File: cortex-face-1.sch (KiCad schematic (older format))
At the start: 14 parts

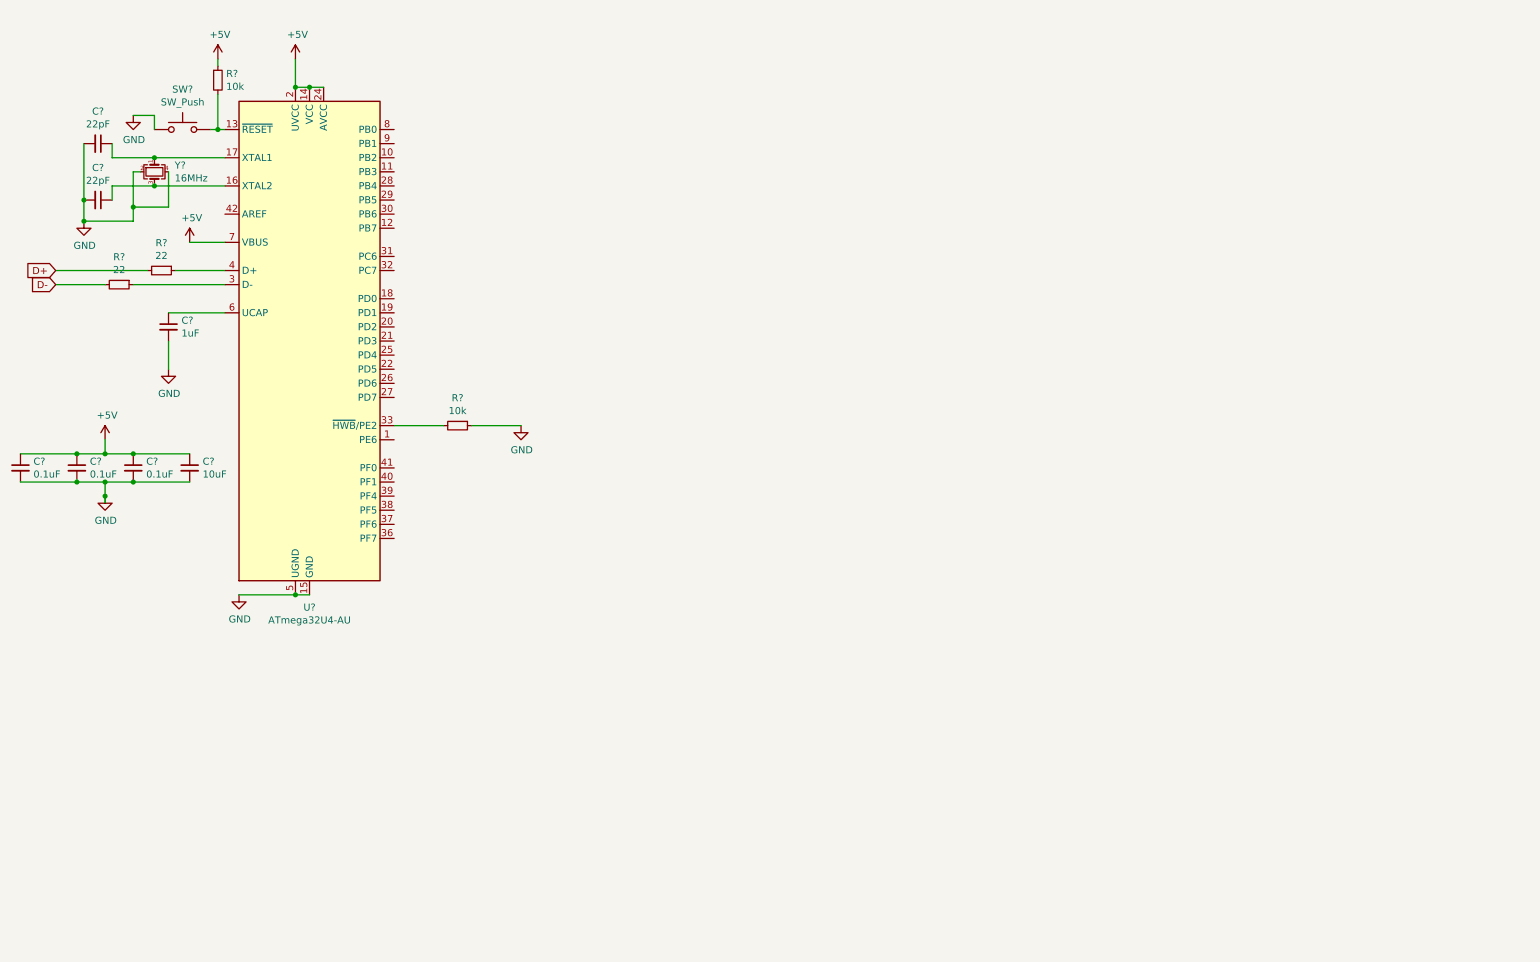
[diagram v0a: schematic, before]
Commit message: Basic 15x6 switch matrix
Switch matrix drawn with a simple rectangular matrix (15x6). MX only switches, no LED support.
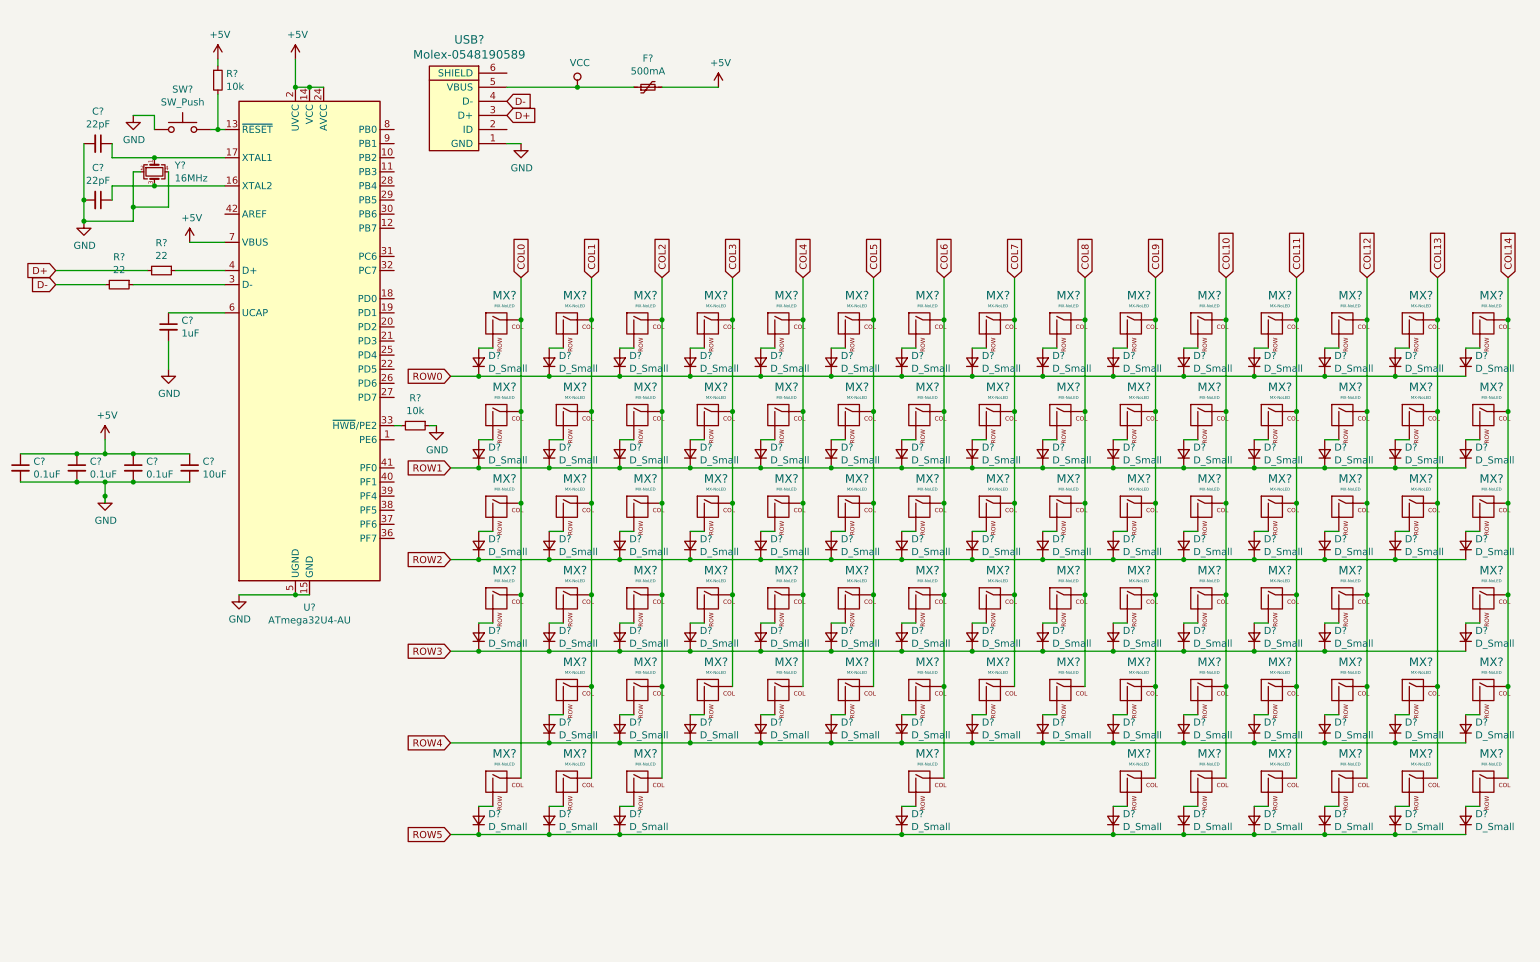
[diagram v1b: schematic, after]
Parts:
- added D? (x83): D_Small, symbol Device:D_Small
- added F?: 500mA, symbol Device:Polyfuse_Small
- added MX? (x83): MX-NoLED, symbol MX_Alps_Hybrid:MX-NoLED
- added USB?: Molex-0548190589, symbol random-keyboard-parts:Molex-0548190589
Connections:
- net +5V: now also F?.2
- net D+: now also USB?.3 (D+)
- net D-: now also USB?.4 (D-)
- net GND: now also USB?.1 (GND)
- new net: D?.2 (A), MX?.2 (ROW) (x83)
- new net COL0: MX?.1 (COL), MX?.1 (COL), MX?.1 (COL), MX?.1 (COL), MX?.1 (COL)
- new net COL1: MX?.1 (COL), MX?.1 (COL), MX?.1 (COL), MX?.1 (COL), MX?.1 (COL), MX?.1 (COL)
- new net COL10: MX?.1 (COL), MX?.1 (COL), MX?.1 (COL), MX?.1 (COL), MX?.1 (COL), MX?.1 (COL)
- new net COL11: MX?.1 (COL), MX?.1 (COL), MX?.1 (COL), MX?.1 (COL), MX?.1 (COL), MX?.1 (COL)
- new net COL12: MX?.1 (COL), MX?.1 (COL), MX?.1 (COL), MX?.1 (COL), MX?.1 (COL), MX?.1 (COL)
- new net COL13: MX?.1 (COL), MX?.1 (COL), MX?.1 (COL), MX?.1 (COL), MX?.1 (COL)
- new net COL14: MX?.1 (COL), MX?.1 (COL), MX?.1 (COL), MX?.1 (COL), MX?.1 (COL), MX?.1 (COL)
- new net COL2: MX?.1 (COL), MX?.1 (COL), MX?.1 (COL), MX?.1 (COL), MX?.1 (COL), MX?.1 (COL)
- new net COL3: MX?.1 (COL), MX?.1 (COL), MX?.1 (COL), MX?.1 (COL), MX?.1 (COL)
- new net COL4: MX?.1 (COL), MX?.1 (COL), MX?.1 (COL), MX?.1 (COL), MX?.1 (COL)
- new net COL5: MX?.1 (COL), MX?.1 (COL), MX?.1 (COL), MX?.1 (COL), MX?.1 (COL)
- new net COL6: MX?.1 (COL), MX?.1 (COL), MX?.1 (COL), MX?.1 (COL), MX?.1 (COL), MX?.1 (COL)
- new net COL7: MX?.1 (COL), MX?.1 (COL), MX?.1 (COL), MX?.1 (COL), MX?.1 (COL)
- new net COL8: MX?.1 (COL), MX?.1 (COL), MX?.1 (COL), MX?.1 (COL), MX?.1 (COL)
- new net COL9: MX?.1 (COL), MX?.1 (COL), MX?.1 (COL), MX?.1 (COL), MX?.1 (COL), MX?.1 (COL)
- new net ROW0: D?.1 (K), D?.1 (K), D?.1 (K), D?.1 (K), D?.1 (K), D?.1 (K), D?.1 (K), D?.1 (K), D?.1 (K), D?.1 (K), D?.1 (K), D?.1 (K), D?.1 (K), D?.1 (K), D?.1 (K)
- new net ROW1: D?.1 (K), D?.1 (K), D?.1 (K), D?.1 (K), D?.1 (K), D?.1 (K), D?.1 (K), D?.1 (K), D?.1 (K), D?.1 (K), D?.1 (K), D?.1 (K), D?.1 (K), D?.1 (K), D?.1 (K)
- new net ROW2: D?.1 (K), D?.1 (K), D?.1 (K), D?.1 (K), D?.1 (K), D?.1 (K), D?.1 (K), D?.1 (K), D?.1 (K), D?.1 (K), D?.1 (K), D?.1 (K), D?.1 (K), D?.1 (K), D?.1 (K)
- new net ROW3: D?.1 (K), D?.1 (K), D?.1 (K), D?.1 (K), D?.1 (K), D?.1 (K), D?.1 (K), D?.1 (K), D?.1 (K), D?.1 (K), D?.1 (K), D?.1 (K), D?.1 (K), D?.1 (K)
- new net ROW4: D?.1 (K), D?.1 (K), D?.1 (K), D?.1 (K), D?.1 (K), D?.1 (K), D?.1 (K), D?.1 (K), D?.1 (K), D?.1 (K), D?.1 (K), D?.1 (K), D?.1 (K), D?.1 (K)
- new net ROW5: D?.1 (K), D?.1 (K), D?.1 (K), D?.1 (K), D?.1 (K), D?.1 (K), D?.1 (K), D?.1 (K), D?.1 (K), D?.1 (K)
- new net VCC: F?.1, USB?.5 (VBUS)
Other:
- moved on the sheet: R?

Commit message: Annotated schematic
Annotated schematic without any assigned footprints
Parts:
- gave numbers to parts that had none: 182

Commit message: Footprints assigned
Footprints (including non-standard key sizes) assigned using MX-Alps Hybrid submodule
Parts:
- C1, C2, C3, C4, C5, C6, C7: footprint (none) -> Capacitor_SMD:C_0805_2012Metric
- D1, D10, D11, D12, D13, D14, D15, D16, D17, D18, D19, D2, D20, D21, D22, D23, D24, D25, D26, D27, D28, D29, D3, D30, D31, D32, D33, D34, D35, D36, D37, D38, D39, D4, D40, D41, D42, D43, D44, D45, D46, D47, D48, D49, D5, D50, D51, D52, D53, D54, D55, D56, D57, D58, D59, D6, D60, D61, D62, D63, D64, D65, D66, D67, D68, D69, D7, D70, D71, D72, D73, D74, D75, D76, D77, D78, D79, D8, D80, D81, D82, D83, D9: footprint (none) -> Diode_SMD:D_SOD-123
- F1: footprint (none) -> Fuse:Fuse_1206_3216Metric
- MX1, MX3, MX75, MX78: footprint (none) -> MX_Alps_Hybrid:MX-1.5U-NoLED
- MX10, MX12, MX13, MX14, MX15, MX16, MX18, MX19, MX2, MX20, MX21, MX22, MX23, MX24, MX25, MX26, MX27, MX28, MX29, MX30, MX31, MX32, MX33, MX34, MX35, MX36, MX37, MX39, MX40, MX41, MX42, MX43, MX44, MX45, MX46, MX47, MX48, MX49, MX50, MX51, MX52, MX53, MX54, MX55, MX56, MX57, MX58, MX59, MX6, MX60, MX61, MX62, MX63, MX64, MX65, MX66, MX67, MX68, MX69, MX7, MX72, MX73, MX76, MX77, MX79, MX8, MX80, MX81, MX82, MX83, MX9: footprint (none) -> MX_Alps_Hybrid:MX-1U-NoLED
- MX11, MX17, MX5: footprint (none) -> MX_Alps_Hybrid:MX-1.25U-NoLED
- MX38: footprint (none) -> MX_Alps_Hybrid:MX-6.25U-NoLED
- MX4, MX71: footprint (none) -> MX_Alps_Hybrid:MX-1.75U-NoLED
- MX70: footprint (none) -> MX_Alps_Hybrid:MX-2.25U-NoLED
- MX74: footprint (none) -> MX_Alps_Hybrid:MX-2U-NoLED
- R1, R2, R3, R4: footprint (none) -> Resistor_SMD:R_0805_2012Metric
- SW1: footprint (none) -> random-keyboard-parts:SKQG-1155865
- USB1: footprint (none) -> random-keyboard-parts:Molex-0548190589
- Y1: footprint (none) -> Crystal:Crystal_SMD_3225-4Pin_3.2x2.5mm

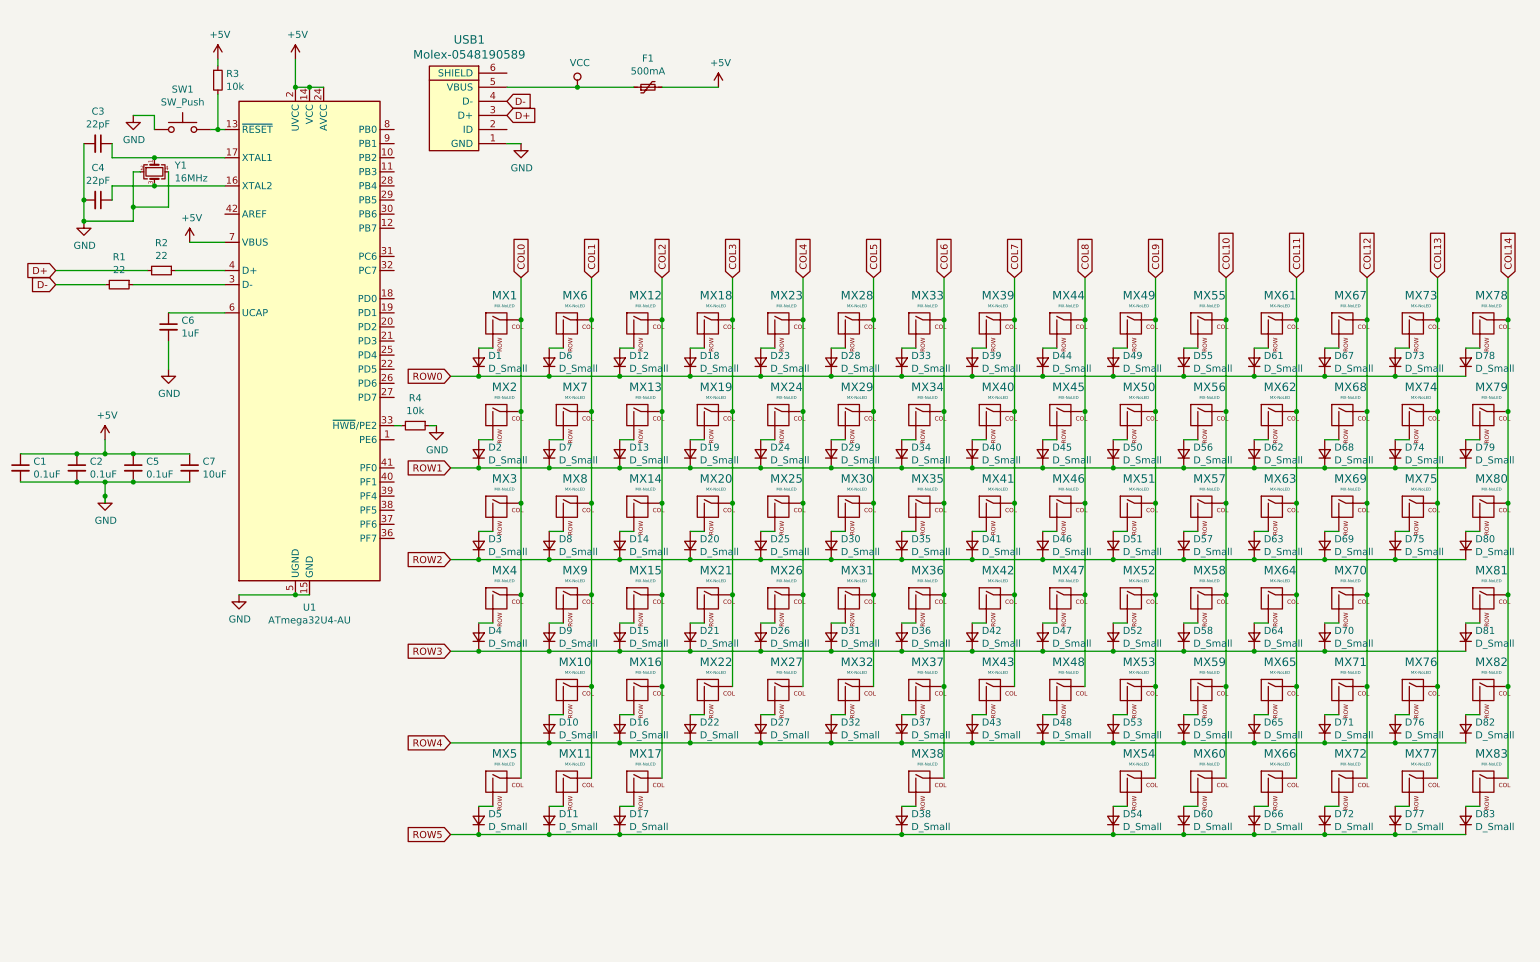
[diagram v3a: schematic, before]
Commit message: Added Pro Micro
Added a rough Pro Micro to the schematic, but have not yet edited the matrix to be compatible. NOT a final Pro Micro schematic.
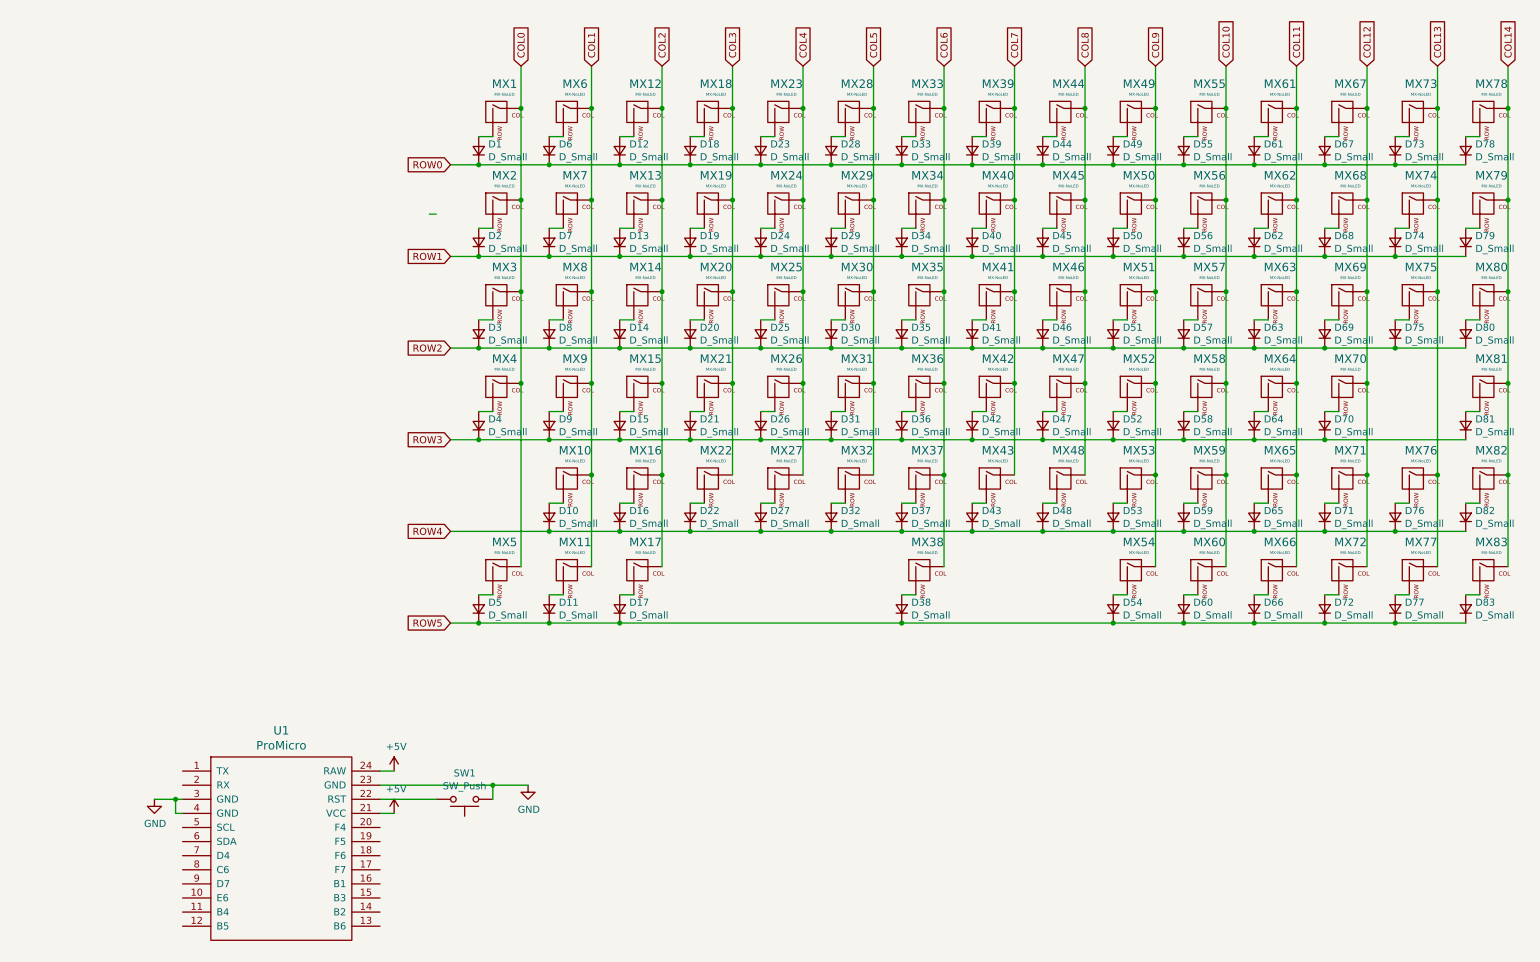
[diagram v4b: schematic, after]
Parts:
- removed C1, C2, C5: 0.1uF, Capacitor_SMD:C_0805_2012Metric, symbol Device:C_Small
- removed C3, C4: 22pF, Capacitor_SMD:C_0805_2012Metric, symbol Device:C_Small
- removed C6: 1uF, Capacitor_SMD:C_0805_2012Metric, symbol Device:C_Small
- removed C7: 10uF, Capacitor_SMD:C_0805_2012Metric, symbol Device:C_Small
- removed F1: 500mA, Fuse:Fuse_1206_3216Metric, symbol Device:Polyfuse_Small
- removed R1, R2: 22, Resistor_SMD:R_0805_2012Metric, symbol Device:R_Small
- removed R3, R4: 10k, Resistor_SMD:R_0805_2012Metric, symbol Device:R_Small
- removed U1: ATmega32U4-AU, Package_QFP:TQFP-44_10x10mm_P0.8mm, symbol MCU_Microchip_ATmega:ATmega32U4-AU
- removed USB1: Molex-0548190589, random-keyboard-parts:Molex-0548190589, symbol random-keyboard-parts:Molex-0548190589
- removed Y1: 16MHz, Crystal:Crystal_SMD_3225-4Pin_3.2x2.5mm, symbol Device:Crystal_GND24_Small
- added U1: ProMicro, symbol promicro:ProMicro
- SW1: footprint random-keyboard-parts:SKQG-1155865 -> (none)
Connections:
- net +5V: now also U1.21 (VCC), U1.24 (RAW)
- net GND: now also U1.23 (GND), U1.3 (GND), U1.4 (GND)
- net at SW1.2: now also U1.22 (RST)
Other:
- moved on the sheet: D1, D10, D11, D12, D13, D14, D15, D16, D17, D18, D19, D2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

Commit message: Pro Micro and USB JCON powered
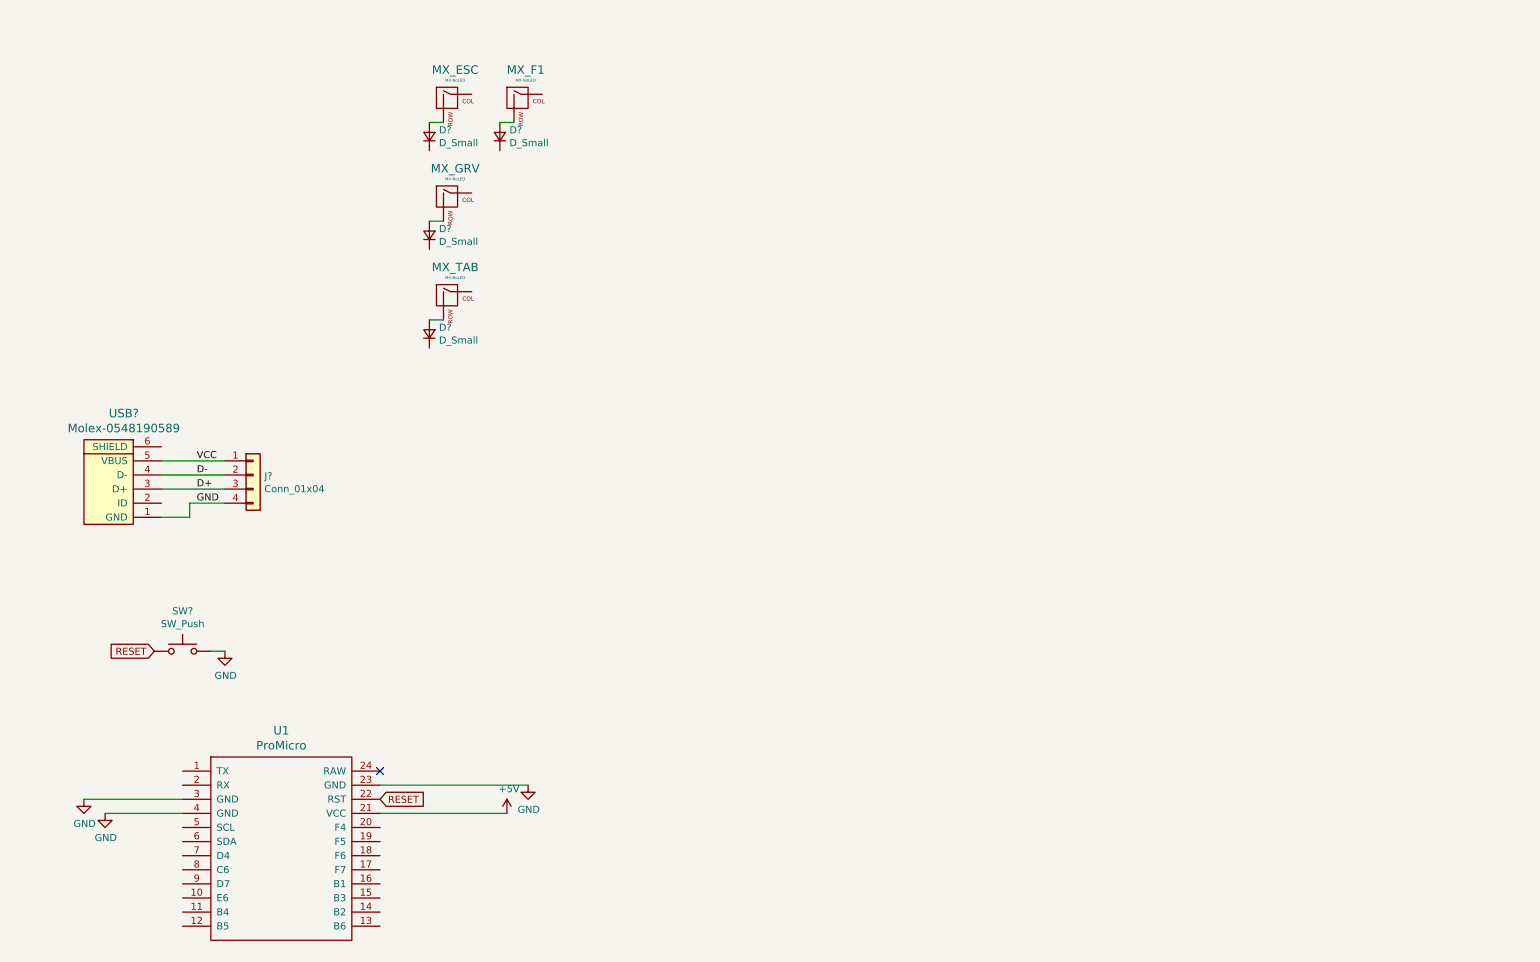
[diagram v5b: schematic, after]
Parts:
- removed D1, D10, D11, D12, D13, D14, D15, D16, D17, D18, D19, D2, D20, D21, D22, D23, D24, D25, D26, D27, D28, D29, D3, D30, D31, D32, D33, D34, D35, D36, D37, D38, D39, D4, D40, D41, D42, D43, D44, D45, D46, D47, D48, D49, D5, D50, D51, D52, D53, D54, D55, D56, D57, D58, D59, D6, D60, D61, D62, D63, D64, D65, D66, D67, D68, D69, D7, D70, D71, D72, D73, D74, D75, D76, D77, D78, D79, D8, D80, D81, D82, D83, D9: D_Small, Diode_SMD:D_SOD-123, symbol Device:D_Small
- removed MX1, MX3, MX75, MX78: MX-NoLED, MX_Alps_Hybrid:MX-1.5U-NoLED, symbol MX_Alps_Hybrid:MX-NoLED
- removed MX10, MX12, MX13, MX14, MX15, MX16, MX18, MX19, MX2, MX20, MX21, MX22, MX23, MX24, MX25, MX26, MX27, MX28, MX29, MX30, MX31, MX32, MX33, MX34, MX35, MX36, MX37, MX39, MX40, MX41, MX42, MX43, MX44, MX45, MX46, MX47, MX48, MX49, MX50, MX51, MX52, MX53, MX54, MX55, MX56, MX57, MX58, MX59, MX6, MX60, MX61, MX62, MX63, MX64, MX65, MX66, MX67, MX68, MX69, MX7, MX72, MX73, MX76, MX77, MX79, MX8, MX80, MX81, MX82, MX83, MX9: MX-NoLED, MX_Alps_Hybrid:MX-1U-NoLED, symbol MX_Alps_Hybrid:MX-NoLED
- removed MX11, MX17, MX5: MX-NoLED, MX_Alps_Hybrid:MX-1.25U-NoLED, symbol MX_Alps_Hybrid:MX-NoLED
- removed MX38: MX-NoLED, MX_Alps_Hybrid:MX-6.25U-NoLED, symbol MX_Alps_Hybrid:MX-NoLED
- removed MX4, MX71: MX-NoLED, MX_Alps_Hybrid:MX-1.75U-NoLED, symbol MX_Alps_Hybrid:MX-NoLED
- removed MX70: MX-NoLED, MX_Alps_Hybrid:MX-2.25U-NoLED, symbol MX_Alps_Hybrid:MX-NoLED
- removed MX74: MX-NoLED, MX_Alps_Hybrid:MX-2U-NoLED, symbol MX_Alps_Hybrid:MX-NoLED
- removed SW1: SW_Push, symbol Switch:SW_Push
- added D? (x4): D_Small, symbol Device:D_Small
- added J?: Conn_01x04, symbol Connector_Generic:Conn_01x04
- added MX_ESC, MX_F1, MX_GRV, MX_TAB: MX-NoLED, symbol MX_Alps_Hybrid:MX-NoLED
- added SW?: SW_Push, symbol Switch:SW_Push
- added USB?: Molex-0548190589, symbol random-keyboard-parts:Molex-0548190589
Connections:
- net +5V: no longer U1.24 (RAW)
- net GND: now also J?.4 (Pin_4), SW?.2, USB?.1 (GND)
- net RESET: now reaches U1.22 (RST)
- net RESET: now also SW?.1
- new net: D?.2 (A), MX_F1.2 (ROW)
- new net: D?.2 (A), MX_ESC.2 (ROW)
- new net: D?.2 (A), MX_GRV.2 (ROW)
- new net: D?.2 (A), MX_TAB.2 (ROW)
- new net D+: J?.3 (Pin_3), USB?.3 (D+)
- new net D-: J?.2 (Pin_2), USB?.4 (D-)
- new net VCC: J?.1 (Pin_1), USB?.5 (VBUS)
- no-connect marks 0 -> 1
